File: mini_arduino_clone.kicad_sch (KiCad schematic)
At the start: 25 parts, among them J101 USB_B_Micro, J103 Conn_01x13, J104 Conn_01x13, J5 Conn_02x03_Odd_Even, SW1 SW_Push, U101 ATmega328P-AU, Y101 16MHz

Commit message: update layout and schematics
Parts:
- removed R14 (x2): 1K, Resistor_SMD:R_0603_1608Metric, symbol Device:R_Small
- added D1: MSS1P4, Diode_SMD:D_MicroSMP_AK, symbol Device:D_Schottky_Small
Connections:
- net +5V: now also J5.2 (VCC), D1.1 (K); no longer F101.2
- net AREF: no longer J104.13 (Pin_13)
- net D10: now also J103.6 (Pin_6); no longer J103.13 (Pin_13)
- net D11/MOSI: now also J103.7 (Pin_7); no longer J103.14 (Pin_14)
- net D12/MISO: now also J103.8 (Pin_8); no longer J103.15 (Pin_15)
- net D13/SCK: now also J104.1 (Pin_1); no longer J104.15 (Pin_15)
- net D2: now also J103.11 (Pin_11); no longer J103.5 (Pin_5)
- net D3: now also J103.10 (Pin_10); no longer J103.6 (Pin_6)
- net D4: now also J103.9 (Pin_9); no longer J103.7 (Pin_7)
- net D5: now also J103.1 (Pin_1); no longer J103.8 (Pin_8)
- net D6: now also J103.2 (Pin_2); no longer J103.9 (Pin_9)
- net D7: now also J103.3 (Pin_3); no longer J103.10 (Pin_10)
- net D8: now also J103.4 (Pin_4); no longer J103.11 (Pin_11)
- net D9: now also J103.5 (Pin_5); no longer J103.12 (Pin_12)
- net GND: now also J103.12 (Pin_12), J104.13 (Pin_13); no longer J103.4 (Pin_4)
- net VBUS: now also J104.15 (Pin_15); no longer J104.1 (Pin_1), J5.2 (VCC)
- net ~{RESET}: now also J103.13 (Pin_13); no longer J103.3 (Pin_3)
- net RX renamed D0/RX
- net D0/RX: now also J103.14 (Pin_14); no longer J103.2 (Pin_2)
- net TX renamed D1/TX
- net D1/TX: now also J103.15 (Pin_15); no longer J103.1 (Pin_1)
- new net USB_UART/VBUS: D1.2 (A), F101.2
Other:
- note added: "Impendance Control for USB"
- note added: "Impendence calculation at JLCPCB Impedance value: 90 ohm Layer: 4-Layer (Impendence stackup JLC7628) Thickness: 1.6mm Inner/Outer layer: outer Impedance type: Differential Trace space: 7 mil Calculated recommended trace width: 9.72 mil"
- company: (none) -> RIT
- title: (none) -> Arduino Nano Clone
- moved on the sheet: F101, J104

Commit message: update parts
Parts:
- D1: value MSS1P4 -> B5819W; footprint Diode_SMD:D_MicroSMP_AK -> Diode_SMD:D_SOD-123; LCSC C2980309 -> C8598
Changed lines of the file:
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@@
       (effects (font (size 1.27 1.27)))
     )
-    (property "Value" "MSS1P4" (at 48.514 26.67 0)
+    (property "Value" "B5819W" (at 48.514 26.67 0)
       (effects (font (size 1.27 1.27)))
     )
-    (property "Footprint" "Diode_SMD:D_MicroSMP_AK" (at 48.26 29.21 90)
+    (property "Footprint" "Diode_SMD:D_SOD-123" (at 48.26 29.21 90)
       (effects (font (size 1.27 1.27)) hide)
     )
-    (property "Datasheet" "https://datasheet.lcsc.com/lcsc/2204251600_Vishay-Intertech-MSS1P4-M3-89A_C2980309.pdf" (at 48.26 29.21 90)
+    (property "Datasheet" "" (at 48.26 29.21 90)
       (effects (font (size 1.27 1.27)) hide)
     )
-    (property "LCSC" "C2980309" (at 48.26 29.21 0)
+    (property "LCSC" "C8598" (at 48.26 29.21 0)
       (effects (font (size 1.27 1.27)) hide)
     )

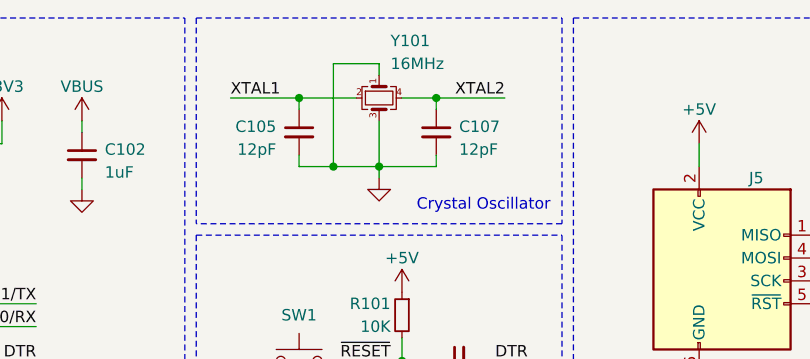
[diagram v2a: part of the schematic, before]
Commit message: fix pin assignments on crystal
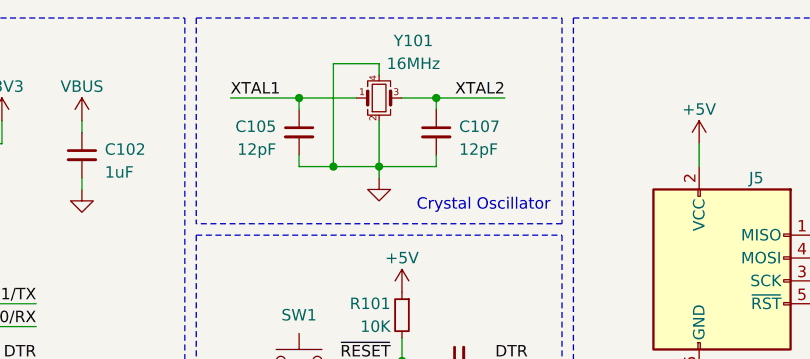
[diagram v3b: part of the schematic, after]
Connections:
- net GND: now also Y101.2, Y101.4; no longer Y101.1, Y101.3
- net XTAL1: now also Y101.1; no longer Y101.2
- net XTAL2: now also Y101.3; no longer Y101.4
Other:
- moved on the sheet: Y101
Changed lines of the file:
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@@
     )
   )
-  (symbol (lib_id "Device:Crystal_GND24_Small") (at 118.11 24.13 270) (unit 1)
+  (symbol (lib_id "Device:Crystal_GND24_Small") (at 118.11 24.13 0) (unit 1)
     (in_bom yes) (on_board yes) (dnp no)
-    (property "Reference" "Y101" (at 119.38 17.78 90)
-      (effects (font (size 1.27 1.27)) (justify left))
+    (property "Reference" "Y101" (at 121.92 17.78 0)
+      (effects (font (size 1.27 1.27)))
     )
-    (property "Value" "16MHz" (at 119.38 20.32 90)
-      (effects (font (size 1.27 1.27)) (justify left))
+    (property "Value" "16MHz" (at 121.92 20.32 0)
+      (effects (font (size 1.27 1.27)))
     )
     (property "Footprint" "Crystal:Crystal_SMD_3225-4Pin_3.2x2.5mm" (at 118.11 24.13 0)
